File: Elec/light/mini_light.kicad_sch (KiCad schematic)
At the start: 18 parts, among them J1 Conn_01x03_MountingPin, J2 Conn_01x03_MountingPin, U1 AL8860WT-7

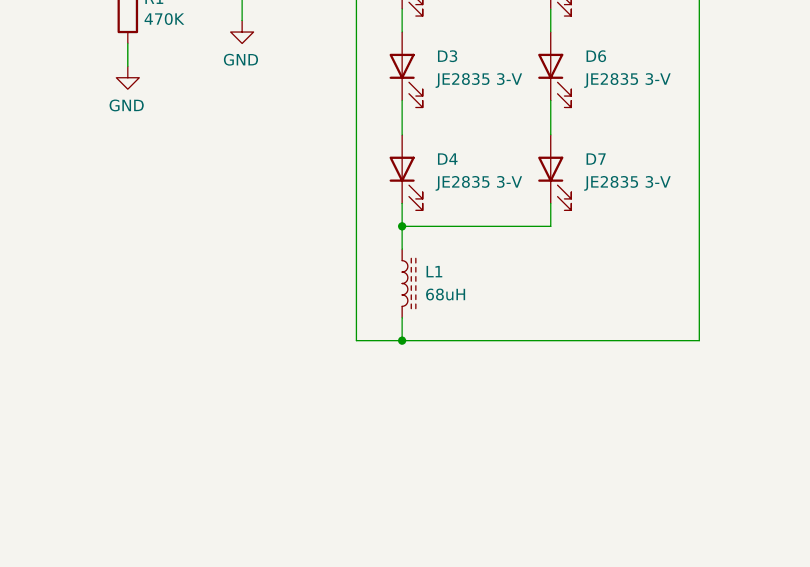
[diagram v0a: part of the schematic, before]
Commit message: delete packages3d folders
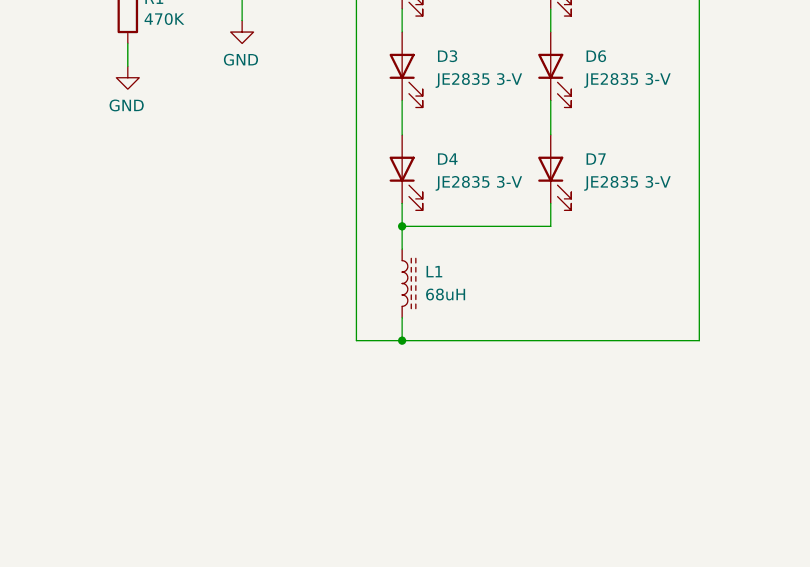
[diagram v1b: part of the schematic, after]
